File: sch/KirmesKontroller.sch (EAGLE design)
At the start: 24 parts, among them IC1 R-78E05-1.0, IC2 YB-ESP32-S3-AMP-V2, IC3 ULN2803, J1 MPE 087-1-003, X2 DG240 2,54-8, X4 DG240 2,54-8, X5 DG240 2,54-2, X6 DG240 2,54-2

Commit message: fix: indexes changed
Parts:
- removed X5: DG240 2,54-2, con-wago255:233-202
- added X3: DG240 2,54-8, con-wago255:233-508
- X2: value DG240 2,54-8 -> DG240 2,54-2; device con-wago255:233-508 -> con-wago255:233-202
- renumbered X6 to X1
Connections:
- net N$11: now also X2.-2; no longer X5.-2
- net N$12: now also X3.-4; no longer X2.-4
- net N$13: now also X3.-3; no longer X2.-3
- net N$14: now also X3.-2; no longer X2.-2
- net N$2: now also X3.-1; no longer X2.-1
- net N$23: now also X3.-8; no longer X2.-8
- net N$4: now also X3.-7; no longer X2.-7
- net N$7: now also X3.-6; no longer X2.-6
- net N$8: now also X3.-5; no longer X2.-5
- net N$9: now also X2.-1; no longer X5.-1
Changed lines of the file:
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@@
 <part name="R2" library="rcl" library_urn="urn:adsk.eagle:library:334" deviceset="R-EU_" device="0207/10" package3d_urn="urn:adsk.eagle:package:23491/2" value="1k5"/>
 <part name="IC3" library="_eigene" deviceset="ULN2803" device="DIL18" value="ULN2803"/>
-<part name="X2" library="con-wago255" library_urn="urn:adsk.eagle:library:198" deviceset="233-508" device="" package3d_urn="urn:adsk.eagle:package:10938/1" value="DG240 2,54-8"/>
+<part name="X3" library="con-wago255" library_urn="urn:adsk.eagle:library:198" deviceset="233-508" device="" package3d_urn="urn:adsk.eagle:package:10938/1" value="DG240 2,54-8"/>
 <part name="X4" library="con-wago255" library_urn="urn:adsk.eagle:library:198" deviceset="233-508" device="" package3d_urn="urn:adsk.eagle:package:10938/1" value="DG240 2,54-8"/>
 <part name="GND6" library="supply1" library_urn="urn:adsk.eagle:library:371" deviceset="GND" device=""/>
 <part name="P+1" library="supply1" library_urn="urn:adsk.eagle:library:371" deviceset="V+" device=""/>
 <part name="P+4" library="supply1" library_urn="urn:adsk.eagle:library:371" deviceset="+5V" device=""/>
-<part name="X5" library="con-wago255" library_urn="urn:adsk.eagle:library:198" deviceset="233-202" device="" package3d_urn="urn:adsk.eagle:package:10884/1" value="DG240 2,54-2"/>
-<part name="X6" library="con-wago255" library_urn="urn:adsk.eagle:library:198" deviceset="233-202" device="" package3d_urn="urn:adsk.eagle:package:10884/1" value="DG240 2,54-2"/>
+<part name="X2" library="con-wago255" library_urn="urn:adsk.eagle:library:198" deviceset="233-202" device="" package3d_urn="urn:adsk.eagle:package:10884/1" value="DG240 2,54-2"/>
+<part name="X1" library="con-wago255" library_urn="urn:adsk.eagle:library:198" deviceset="233-202" device="" package3d_urn="urn:adsk.eagle:package:10884/1" value="DG240 2,54-2"/>
 <part name="J1" library="jumper" library_urn="urn:adsk.eagle:library:252" deviceset="JP2E" device="" package3d_urn="urn:adsk.eagle:package:15452/1" value="MPE 087-1-003"/>
 <part name="P+6" library="supply1" library_urn="urn:adsk.eagle:library:371" deviceset="V+" device=""/>
@@
 <attribute name="VALUE" x="205.74" y="43.18" size="1.27" layer="96"/>
 </instance>
-<instance part="X2" gate="G$1" x="248.92" y="83.82" smashed="yes" rot="R90">
+<instance part="X3" gate="G$1" x="248.92" y="83.82" smashed="yes" rot="R90">
 <attribute name="NAME" x="238.76" y="78.74" size="1.778" layer="95" rot="R90"/>
 <attribute name="VALUE" x="241.3" y="85.09" size="1.778" layer="96"/>
@@
 <attribute name="VALUE" x="139.7" y="236.22" size="1.778" layer="96" rot="R90"/>
 </instance>
-<instance part="X5" gate="G$1" x="30.48" y="124.46" smashed="yes" rot="MR0">
+<instance part="X2" gate="G$1" x="30.48" y="124.46" smashed="yes" rot="MR0">
 <attribute name="NAME" x="35.56" y="127" size="1.778" layer="95" rot="MR0"/>
 <attribute name="VALUE" x="29.21" y="127" size="1.778" layer="96" rot="MR270"/>
 </instance>
-<instance part="X6" gate="G$1" x="25.4" y="243.84" smashed="yes" rot="MR0">
+<instance part="X1" gate="G$1" x="25.4" y="243.84" smashed="yes" rot="MR0">
 <attribute name="NAME" x="30.48" y="246.38" size="1.778" layer="95" rot="MR0"/>
 <attribute name="VALUE" x="24.13" y="246.38" size="1.778" layer="96" rot="MR270"/>
@@
 <wire x1="63.5" y1="231.14" x2="63.5" y2="228.6" width="0.1524" layer="91"/>
 <wire x1="63.5" y1="228.6" x2="33.02" y2="228.6" width="0.1524" layer="91"/>
-<pinref part="X6" gate="G$1" pin="-2"/>
+<pinref part="X1" gate="G$1" pin="-2"/>
 <wire x1="33.02" y1="241.3" x2="33.02" y2="228.6" width="0.1524" layer="91"/>
 </segment>
@@
 <segment>
 <pinref part="R2" gate="G$1" pin="1"/>
-<pinref part="X5" gate="G$1" pin="-1"/>
+<pinref part="X2" gate="G$1" pin="-1"/>
 <wire x1="38.1" y1="124.46" x2="66.04" y2="124.46" width="0.1524" layer="91"/>
 </segment>
@@
 <wire x1="88.9" y1="116.84" x2="38.1" y2="116.84" width="0.1524" layer="91"/>
 <wire x1="38.1" y1="116.84" x2="38.1" y2="121.92" width="0.1524" layer="91"/>
-<pinref part="X5" gate="G$1" pin="-2"/>
+<pinref part="X2" gate="G$1" pin="-2"/>
 </segment>
 </net>
@@
 <segment>
 <pinref part="IC3" gate="G$1" pin="OUT8"/>
-<pinref part="X2" gate="G$1" pin="-8"/>
+<pinref part="X3" gate="G$1" pin="-8"/>
 <wire x1="231.14" y1="53.34" x2="259.08" y2="53.34" width="0.1524" layer="91"/>
 <wire x1="259.08" y1="53.34" x2="259.08" y2="76.2" width="0.1524" layer="91"/>
@@
 <net name="N$15" class="0">
 <segment>
-<pinref part="X6" gate="G$1" pin="-1"/>
+<pinref part="X1" gate="G$1" pin="-1"/>
 <pinref part="F1" gate="1" pin="1"/>
 <wire x1="33.02" y1="243.84" x2="40.64" y2="243.84" width="0.1524" layer="91"/>
@@
 <segment>
 <pinref part="IC3" gate="G$1" pin="OUT1"/>
-<pinref part="X2" gate="G$1" pin="-1"/>
+<pinref part="X3" gate="G$1" pin="-1"/>
 <wire x1="231.14" y1="71.12" x2="241.3" y2="71.12" width="0.1524" layer="91"/>
 <wire x1="241.3" y1="71.12" x2="241.3" y2="76.2" width="0.1524" layer="91"/>
@@
 <segment>
 <pinref part="IC3" gate="G$1" pin="OUT7"/>
-<pinref part="X2" gate="G$1" pin="-7"/>
+<pinref part="X3" gate="G$1" pin="-7"/>
 <wire x1="231.14" y1="55.88" x2="256.54" y2="55.88" width="0.1524" layer="91"/>
 <wire x1="256.54" y1="55.88" x2="256.54" y2="76.2" width="0.1524" layer="91"/>
@@
 <segment>
 <pinref part="IC3" gate="G$1" pin="OUT6"/>
-<pinref part="X2" gate="G$1" pin="-6"/>
+<pinref part="X3" gate="G$1" pin="-6"/>
 <wire x1="231.14" y1="58.42" x2="254" y2="58.42" width="0.1524" layer="91"/>
 <wire x1="254" y1="58.42" x2="254" y2="76.2" width="0.1524" layer="91"/>
@@
 <segment>
 <pinref part="IC3" gate="G$1" pin="OUT5"/>
-<pinref part="X2" gate="G$1" pin="-5"/>
+<pinref part="X3" gate="G$1" pin="-5"/>
 <wire x1="231.14" y1="60.96" x2="251.46" y2="60.96" width="0.1524" layer="91"/>
 <wire x1="251.46" y1="60.96" x2="251.46" y2="76.2" width="0.1524" layer="91"/>
@@
 <segment>
 <pinref part="IC3" gate="G$1" pin="OUT4"/>
-<pinref part="X2" gate="G$1" pin="-4"/>
+<pinref part="X3" gate="G$1" pin="-4"/>
 <wire x1="231.14" y1="63.5" x2="248.92" y2="63.5" width="0.1524" layer="91"/>
 <wire x1="248.92" y1="63.5" x2="248.92" y2="76.2" width="0.1524" layer="91"/>
@@
 <segment>
 <pinref part="IC3" gate="G$1" pin="OUT3"/>
-<pinref part="X2" gate="G$1" pin="-3"/>
+<pinref part="X3" gate="G$1" pin="-3"/>
 <wire x1="231.14" y1="66.04" x2="246.38" y2="66.04" width="0.1524" layer="91"/>
 <wire x1="246.38" y1="66.04" x2="246.38" y2="76.2" width="0.1524" layer="91"/>
@@
 <segment>
 <pinref part="IC3" gate="G$1" pin="OUT2"/>
-<pinref part="X2" gate="G$1" pin="-2"/>
+<pinref part="X3" gate="G$1" pin="-2"/>
 <wire x1="231.14" y1="68.58" x2="243.84" y2="68.58" width="0.1524" layer="91"/>
 <wire x1="243.84" y1="68.58" x2="243.84" y2="76.2" width="0.1524" layer="91"/>

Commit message: initial upload
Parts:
- removed JP1, JP2, JP3, JP4: (no value), jumper:JP2E
- added R4, R5: 10k, rcl:R-EU_0207/10
- added X5, X6, X7, X8: 22-23-2031, con-molex:22-23-2031
- C3, C4: value (none) -> 100n
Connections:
- net GPIO39 renamed RESET
- removed net GPIO2: IC2.IO2, OK1.VO
- removed net N$12: IC3.OUT4, X3.-4
- removed net N$13: IC3.OUT3, X3.-3
- removed net N$14: IC3.OUT2, X3.-2
- removed net N$17: C3.2, C4.2, JP1.3, JP2.3, JP3.3, JP4.1
- removed net N$2: IC3.OUT1, X3.-1
- removed net N$23: IC3.OUT8, X3.-8
- removed net N$4: IC3.OUT7, X3.-7
- removed net N$7: IC3.OUT6, X3.-6
- removed net N$8: IC3.OUT5, X3.-5
- new net DCC: IC2.IO40, OK1.VO
- new net X3_B-1: IC3.OUT1, X3.-1, X3.B-1
- new net X3_B-2: IC3.OUT2, X3.-2, X3.B-2
- new net X3_B-3: IC3.OUT3, X3.-3, X3.B-3
- new net X3_B-4: IC3.OUT4, X3.-4, X3.B-4
- new net X3_B-5: IC3.OUT5, X3.-5, X3.B-5
- new net X3_B-6: IC3.OUT6, X3.-6, X3.B-6
- new net X3_B-7: IC3.OUT7, X3.-7, X3.B-7
- new net X3_B-8: IC3.OUT8, X3.-8, X3.B-8
- net +3V3: now also R4.2, R5.2
- net +5V: now also IC2.5V@1, X5-2.S, X6-2.S, X7-2.S; no longer JP1.2, JP2.2, JP3.2
- net GND: now also C3.2, C4.2, X5-3.S, X6-3.S, X7-3.S, X8-3.S
- net INPUT1: now also IC2.IO47, R5.1, X8-1.S; no longer IC2.IO48, JP4.2
- net INPUT2: now also IC2.IO48, R4.1, X8-2.S; no longer IC2.IO47, JP4.3
- net O21: now also IC2.IO2, X5-1.S; no longer IC2.IO42, JP1.1
- net O22: now also IC2.IO42, X6-1.S; no longer IC2.IO41, JP2.1
- net O23: now also IC2.IO41, X7-1.S; no longer IC2.IO40, JP3.1
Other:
- moved on the sheet: X3

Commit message: Version 1.0
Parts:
- added C5: 100n, rcl:C-EU050-024X044
- added D1, D2: BAT42, diode:BAT42
- added R6, R7: 330R, rcl:R-EU_0207/10
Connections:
- new net N$1: R5.1, R6.2, X8-1.S
- new net N$2: R4.1, R7.2, X8-2.S
- net +5V: now also C5.1
- net GND: now also C5.2, D1.A, D2.A
- net INPUT1: now also D1.C, R6.1; no longer R5.1, X8-1.S
- net INPUT2: now also D2.C, R7.1; no longer R4.1, X8-2.S
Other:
- moved on the sheet: C3, C4, R4, R5, X5-1, X5-2, X5-3, X6-1, X6-2, X6-3, X7-1, X7-2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

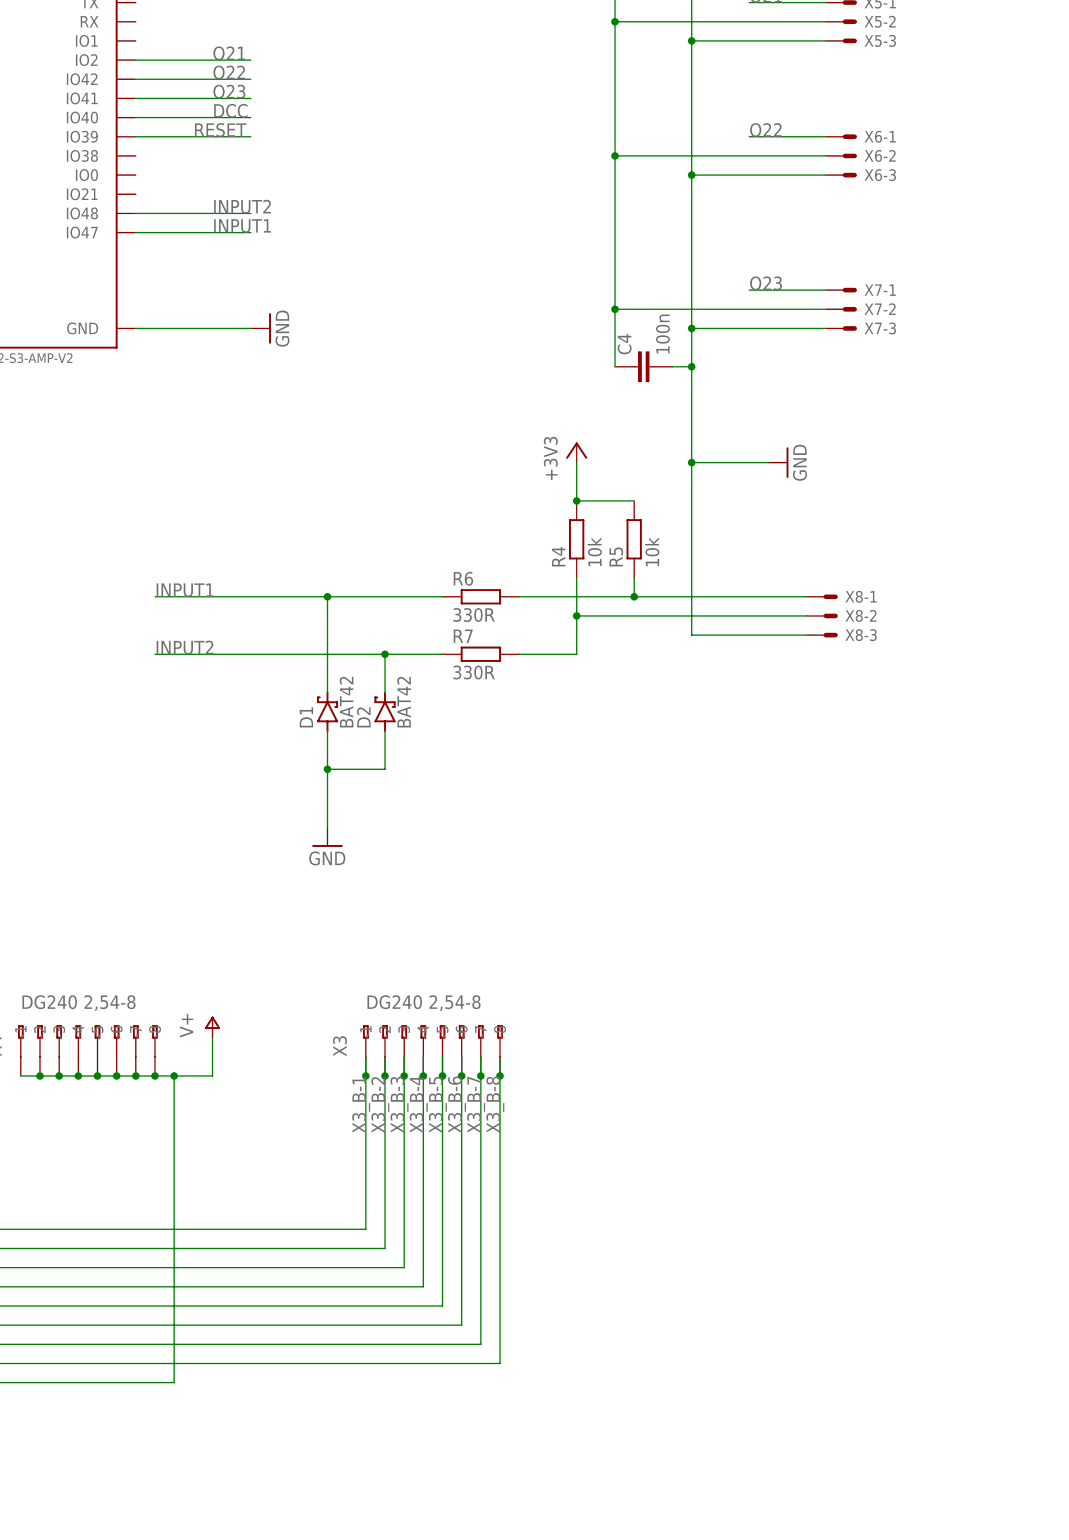
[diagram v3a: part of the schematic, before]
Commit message: fixed pinmapping
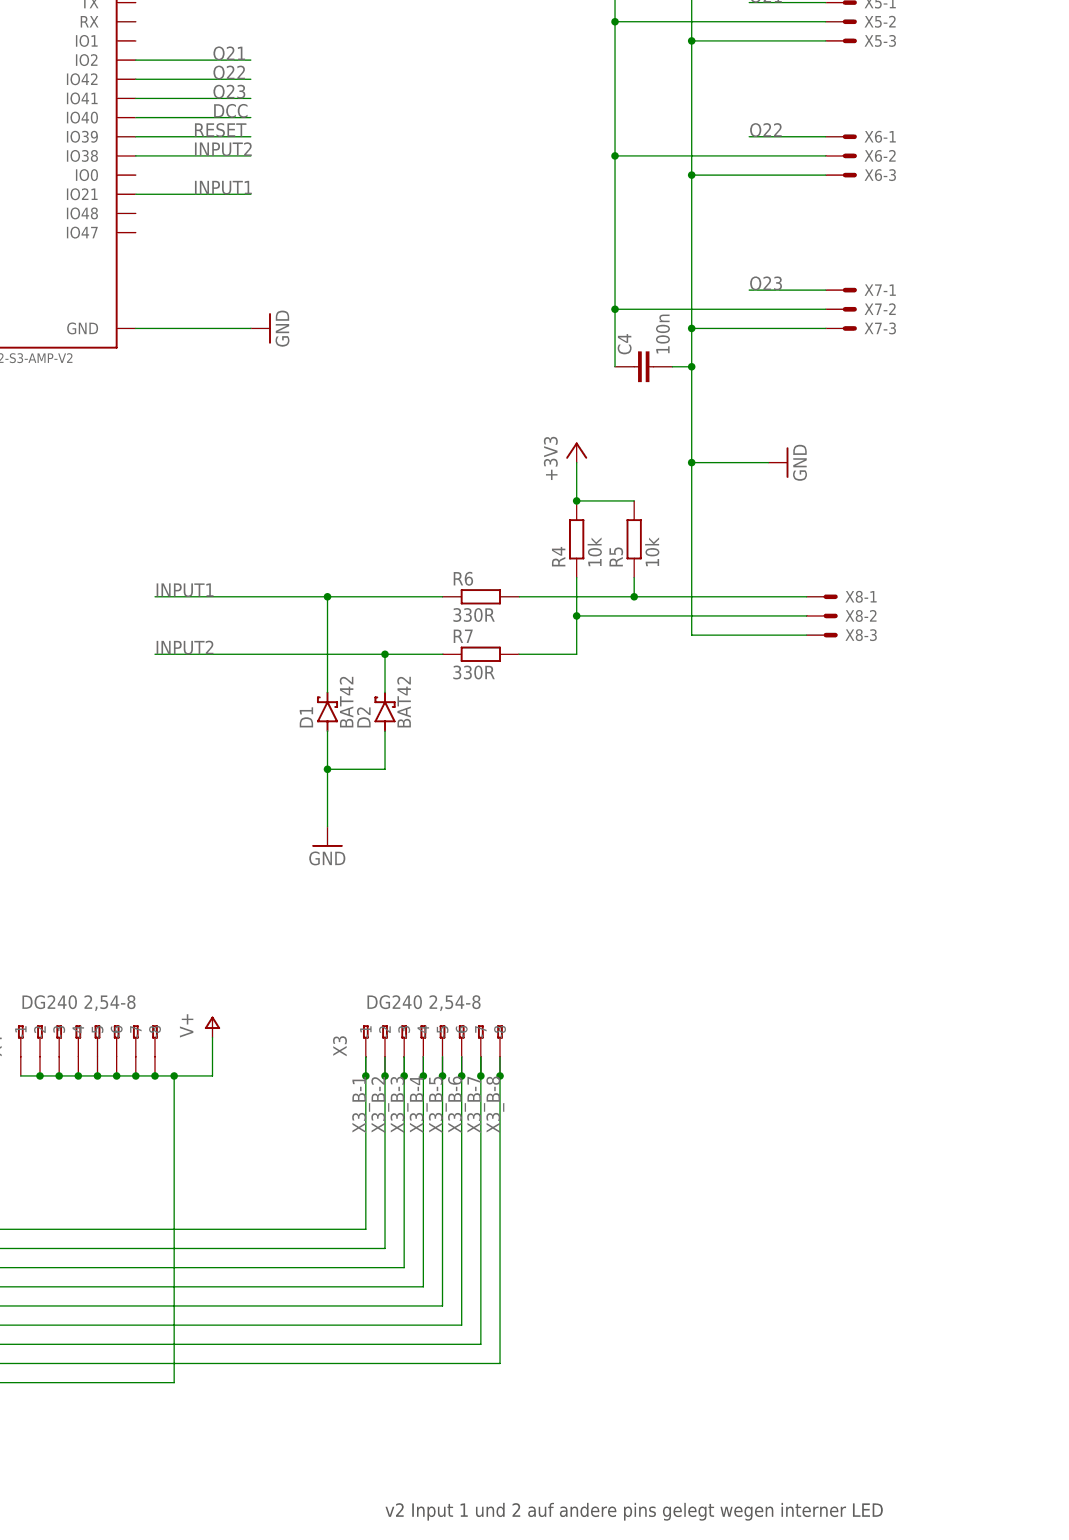
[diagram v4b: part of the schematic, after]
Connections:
- net INPUT1: now also IC2.IO21; no longer IC2.IO47
- net INPUT2: now also IC2.IO38; no longer IC2.IO48
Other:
- note added: "v2 Input 1 und 2 auf andere pins gelegt wegen interner LED"
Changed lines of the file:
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@@
 <text x="20.32" y="233.68" size="1.778" layer="97" rot="R90">7 - 24VAC</text>
 <text x="25.4" y="119.38" size="1.778" layer="97" rot="R90">DCC</text>
+<text x="289.56" y="33.02" size="1.778" layer="97">v2 Input 1 und 2 auf andere pins gelegt wegen interner LED</text>
 </plain>
 <instances>
@@
 <net name="INPUT2" class="0">
 <segment>
-<pinref part="IC2" gate="G$1" pin="IO48"/>
-<wire x1="256.54" y1="205.74" x2="271.78" y2="205.74" width="0.1524" layer="91"/>
-<label x="266.7" y="205.74" size="1.778" layer="95"/>
-</segment>
-<segment>
 <pinref part="R7" gate="G$1" pin="1"/>
 <wire x1="297.18" y1="147.32" x2="289.56" y2="147.32" width="0.1524" layer="91"/>
@@
 <junction x="289.56" y="147.32"/>
 </segment>
+<segment>
+<pinref part="IC2" gate="G$1" pin="IO38"/>
+<wire x1="256.54" y1="213.36" x2="271.78" y2="213.36" width="0.1524" layer="91"/>
+<label x="264.16" y="213.36" size="1.778" layer="95"/>
+</segment>
 </net>
 <net name="INPUT1" class="0">
-<segment>
-<pinref part="IC2" gate="G$1" pin="IO47"/>
-<wire x1="256.54" y1="203.2" x2="271.78" y2="203.2" width="0.1524" layer="91"/>
-<label x="266.7" y="203.2" size="1.778" layer="95"/>
-</segment>
 <segment>
 <pinref part="R6" gate="G$1" pin="1"/>
@@
 <junction x="281.94" y="154.94"/>
 </segment>
-</net>
+<segment>
+<pinref part="IC2" gate="G$1" pin="IO21"/>
+<wire x1="256.54" y1="208.28" x2="271.78" y2="208.28" width="0.1524" layer="91"/>
+<label x="264.16" y="208.28" size="1.778" layer="95"/>
+</segment>
+</net>

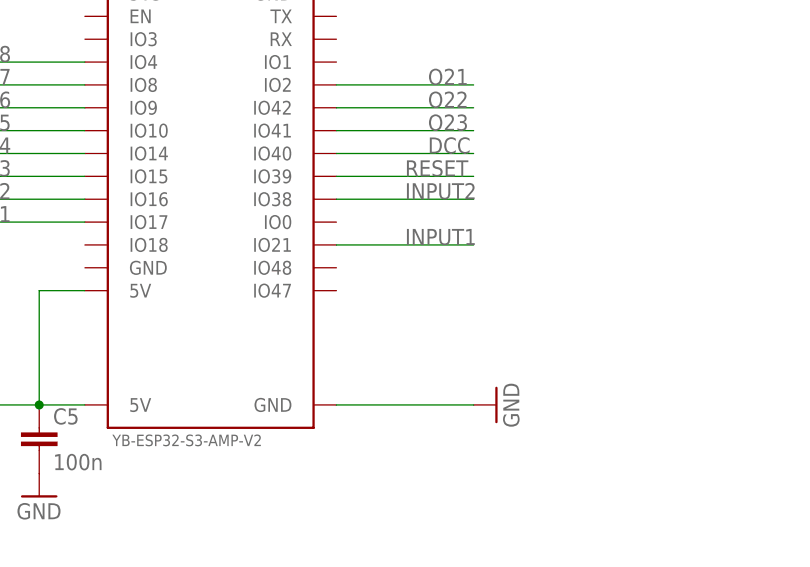
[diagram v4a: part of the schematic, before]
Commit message: pin 47 named
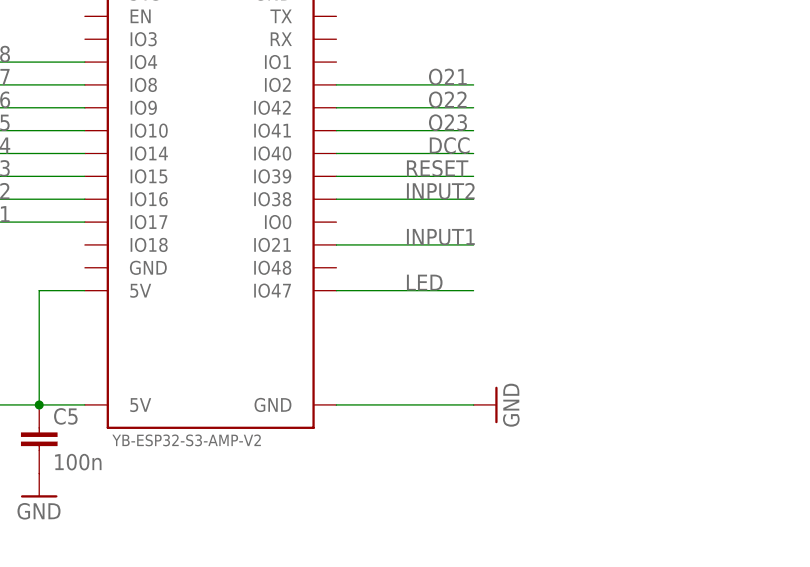
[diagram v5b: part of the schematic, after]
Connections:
- new net LED: IC2.IO47
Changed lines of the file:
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@@
+</segment>
+</net>
+<net name="LED" class="0">
+<segment>
+<pinref part="IC2" gate="G$1" pin="IO47"/>
+<wire x1="256.54" y1="203.2" x2="271.78" y2="203.2" width="0.1524" layer="91"/>
+<label x="264.16" y="203.2" size="1.778" layer="95"/>
 </segment>
 </net>
